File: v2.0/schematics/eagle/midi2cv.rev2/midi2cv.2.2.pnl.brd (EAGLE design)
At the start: 99.4 x 41.9 mm, 22 parts, among them IC1 TL084P, IC2 TL084P, J1 CV3 OUT, J2 CV2 OUT, J3 CV1 OUT, J4 GATE1 OUT, J5 GATE2 OUT, J6 GATE3 OUT, J7 GATE4 OUT, J8 GATE5 OUT

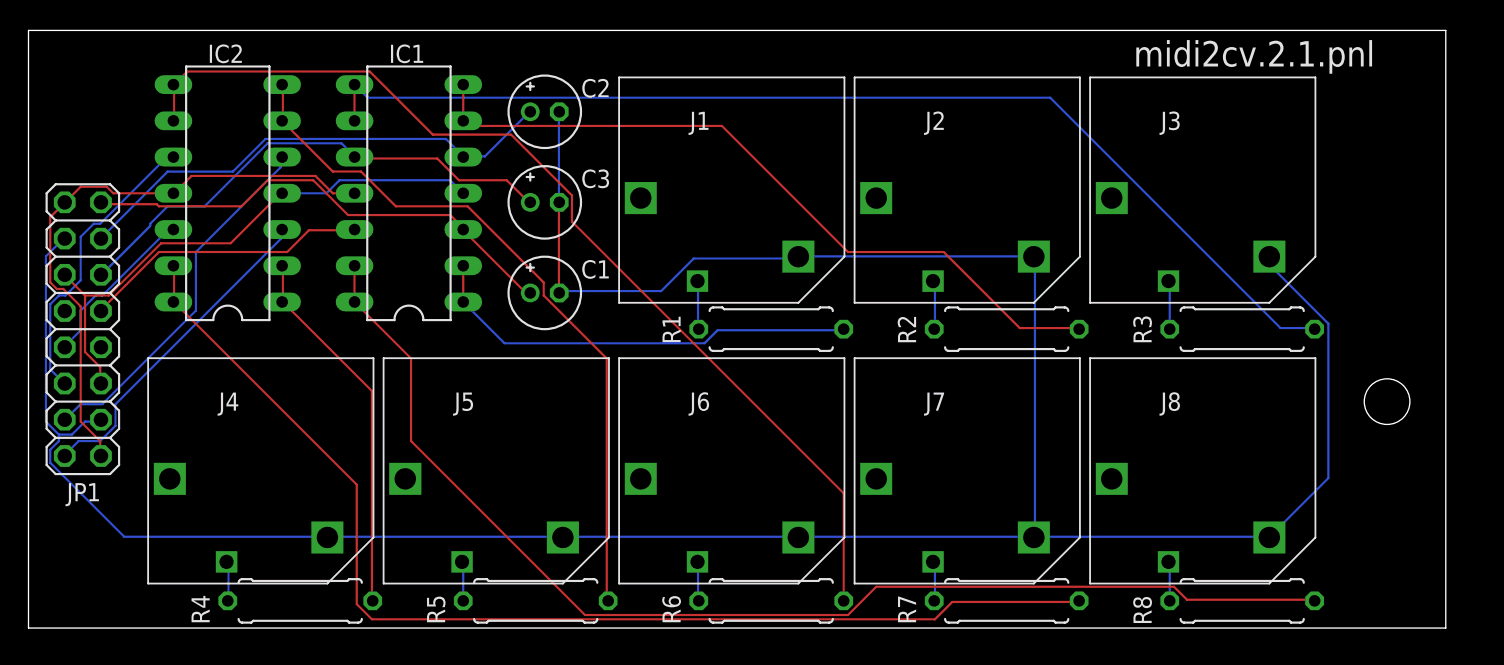
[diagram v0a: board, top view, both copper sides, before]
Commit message: Corrected pin mappings on Jacks Updated midi2cv with new jacks mapping Rerouted main and pnl Increased minimum width in design rules from 6mil to 12mil
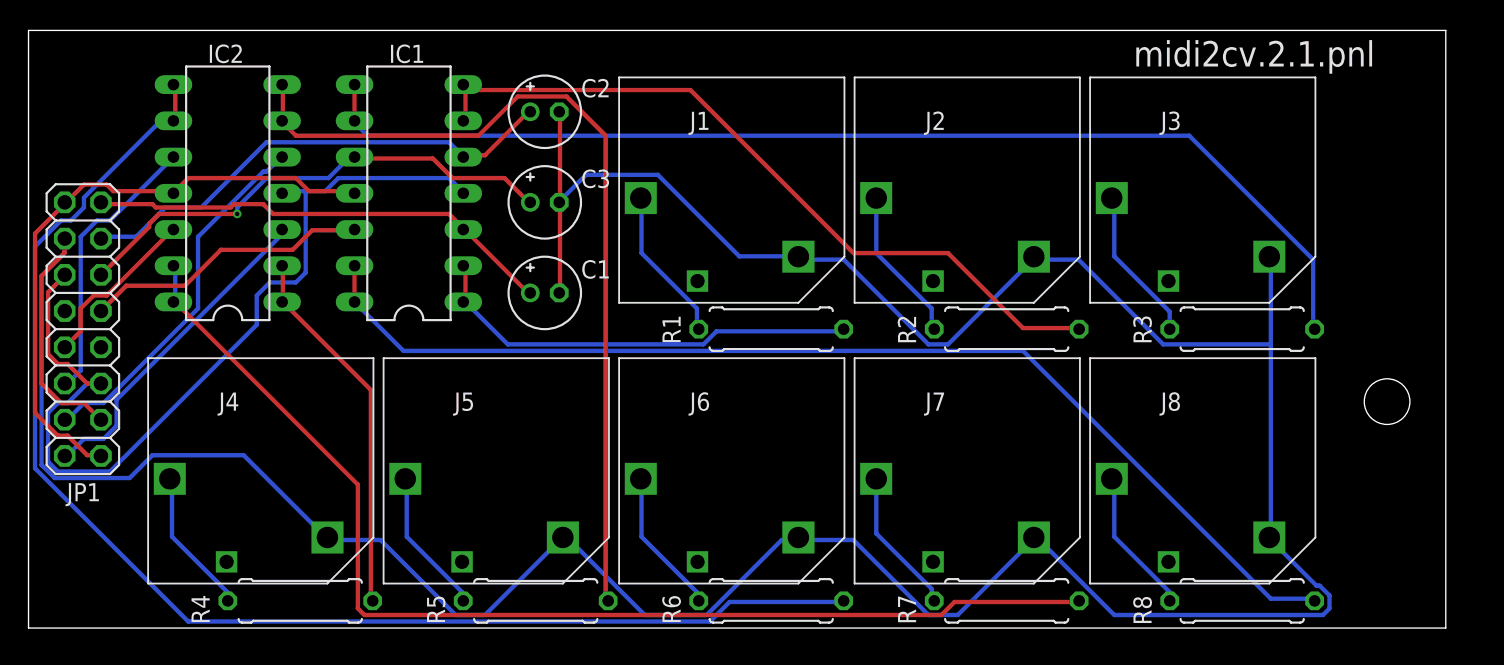
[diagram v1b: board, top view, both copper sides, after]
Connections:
- net N$21: now also J4.P$3; no longer J4.P$2
- net N$22: now also J5.P$3; no longer J5.P$2
- net N$23: now also J6.P$3; no longer J6.P$2
- net N$24: now also J7.P$3; no longer J7.P$2
- net N$25: now also J8.P$3; no longer J8.P$2
- net N$44: now also J1.P$3; no longer J1.P$2
- net N$45: now also J2.P$3; no longer J2.P$2
- net N$46: now also J3.P$3; no longer J3.P$2
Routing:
- net 0V: track 198.0 -> 242.7 mm
- net +12V: track 38.9 -> 63.3 mm
- net N$35: track 70.8 -> 93.7 mm
- net N$36: track 49.8 -> 60.7 mm
- net N$44: track 3.39 -> 10.9 mm
- net N$46: track 3.40 -> 10.9 mm
- net N$25: track 2.78 -> 10.2 mm
- net N$45: track 3.46 -> 10.9 mm
- net N$23: track 2.76 -> 10.2 mm
- net N$22: track 2.78 -> 10.2 mm
- net N$24: track 2.83 -> 10.2 mm
- net N$21: track 2.83 -> 10.2 mm
- net N$7: track 83.6 -> 78.5 mm
- net N$4: track 76.9 -> 78.8 mm
- net -12V: track 41.9 -> 43.6 mm
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
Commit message: Updated version on schem and board to 2.2 Revised labels for GATE1..5 to match board layout and firmare
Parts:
- J4: value GATE1 OUT -> GATE5 OUT
- J5: value GATE2 OUT -> GATE4 OUT
- J7: value GATE4 OUT -> GATE2 OUT
- J8: value GATE5 OUT -> GATE1 OUT
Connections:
- net GATE1: now also IC1.12, JP1.9; no longer IC2.3, JP1.2
- net GATE2: now also IC2.12, JP1.8; no longer IC2.5, JP1.4
- net GATE4: now also IC2.5, JP1.4; no longer IC2.12, JP1.8
- net GATE5: now also IC2.3, JP1.2; no longer IC1.12, JP1.9
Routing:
- net GATE2: track 25.8 -> 11.9 mm
- net GATE4: track 12.0 -> 25.6 mm
- net GATE1: track 23.1 -> 20.1 mm
- net GATE5: track 20.2 -> 22.9 mm
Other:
- board text added: "midi2cv.2.2.pnl"
- board text removed: "midi2cv.2.1.pnl"
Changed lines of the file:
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@@
 <?xml version="1.0" encoding="utf-8"?>
 <!DOCTYPE eagle SYSTEM "eagle.dtd">
-<eagle version="7.5.0">
+<eagle version="7.2.0">
 <drawing>
 <settings>
@@
 <wire x1="99.365" y1="41.9" x2="0" y2="41.9" width="0" layer="20"/>
 <wire x1="0" y1="41.9" x2="0" y2="0" width="0" layer="20"/>
-<text x="77.47" y="39.37" size="1.778" layer="25" font="vector">midi2cv.2.1.pnl</text>
+<text x="77.47" y="39.37" size="1.778" layer="25" font="vector">midi2cv.2.2.pnl</text>
 <hole x="95.25" y="15.875" drill="3.2"/>
 </plain>
@@
 <attribute name="VALUE" x="27.305" y="23.749" size="1.27" layer="27" ratio="10" rot="R90"/>
 </element>
-<element name="J4" library="jacks" package="ACJM-MV35-2S" value="GATE1 OUT" x="20.955" y="6.35" locked="yes"/>
-<element name="J5" library="jacks" package="ACJM-MV35-2S" value="GATE2 OUT" x="37.465" y="6.35" locked="yes"/>
+<element name="J4" library="jacks" package="ACJM-MV35-2S" value="GATE5 OUT" x="20.955" y="6.35" locked="yes"/>
+<element name="J5" library="jacks" package="ACJM-MV35-2S" value="GATE4 OUT" x="37.465" y="6.35" locked="yes"/>
 <element name="J6" library="jacks" package="ACJM-MV35-2S" value="GATE3 OUT" x="53.975" y="6.35" locked="yes"/>
-<element name="J7" library="jacks" package="ACJM-MV35-2S" value="GATE4 OUT" x="70.485" y="6.35" locked="yes"/>
-<element name="J8" library="jacks" package="ACJM-MV35-2S" value="GATE5 OUT" x="86.995" y="6.35" locked="yes"/>
+<element name="J7" library="jacks" package="ACJM-MV35-2S" value="GATE2 OUT" x="70.485" y="6.35" locked="yes"/>
+<element name="J8" library="jacks" package="ACJM-MV35-2S" value="GATE1 OUT" x="86.995" y="6.35" locked="yes"/>
 <element name="J1" library="jacks" package="ACJM-MV35-2S" value="CV3 OUT" x="53.975" y="26.035" locked="yes"/>
 <element name="J2" library="jacks" package="ACJM-MV35-2S" value="CV2 OUT" x="70.485" y="26.035"/>
@@
 <wire x1="76.1238" y1="10.287" x2="75.945" y2="10.46" width="0.3048" layer="16"/>
 </signal>
-<signal name="GATE1">
-<contactref element="JP1" pad="2"/>
-<contactref element="IC2" pad="3"/>
-<wire x1="17.6022" y1="27.432" x2="17.6022" y2="27.8892" width="0.3048" layer="16"/>
-<wire x1="6.1722" y1="16.002" x2="17.6022" y2="27.432" width="0.3048" layer="16"/>
-<wire x1="6.1722" y1="14.1732" x2="6.1722" y2="16.002" width="0.3048" layer="16"/>
-<wire x1="5.2578" y1="13.2588" x2="6.1722" y2="14.1732" width="0.3048" layer="16"/>
-<wire x1="3.8862" y1="13.2588" x2="5.2578" y2="13.2588" width="0.3048" layer="16"/>
-<wire x1="2.7432" y1="12.1158" x2="3.8862" y2="13.2588" width="0.3048" layer="16"/>
-<wire x1="17.6022" y1="27.8892" x2="17.78" y2="27.94" width="0.3048" layer="16"/>
-<wire x1="2.7432" y1="12.1158" x2="2.54" y2="12.065" width="0.3048" layer="16"/>
-</signal>
-<signal name="GATE2">
-<contactref element="JP1" pad="4"/>
-<contactref element="IC2" pad="5"/>
-<wire x1="16.6878" y1="32.004" x2="17.6022" y2="32.9184" width="0.3048" layer="16"/>
-<wire x1="16.4592" y1="32.004" x2="16.6878" y2="32.004" width="0.3048" layer="16"/>
-<wire x1="11.8872" y1="27.432" x2="16.4592" y2="32.004" width="0.3048" layer="16"/>
-<wire x1="11.8872" y1="22.4028" x2="11.8872" y2="27.432" width="0.3048" layer="16"/>
-<wire x1="5.2578" y1="15.7734" x2="11.8872" y2="22.4028" width="0.3048" layer="16"/>
-<wire x1="3.8862" y1="15.7734" x2="5.2578" y2="15.7734" width="0.3048" layer="16"/>
-<wire x1="2.7432" y1="14.6304" x2="3.8862" y2="15.7734" width="0.3048" layer="16"/>
-<wire x1="17.6022" y1="32.9184" x2="17.78" y2="33.02" width="0.3048" layer="16"/>
-<wire x1="2.7432" y1="14.6304" x2="2.54" y2="14.605" width="0.3048" layer="16"/>
-</signal>
 <signal name="GATE3">
 <contactref element="JP1" pad="6"/>
@@
 <wire x1="2.7432" y1="17.145" x2="3.6576" y2="18.0594" width="0.3048" layer="16"/>
 <wire x1="2.7432" y1="17.145" x2="2.54" y2="17.145" width="0.3048" layer="16"/>
-</signal>
-<signal name="GATE4">
-<contactref element="JP1" pad="8"/>
-<contactref element="IC2" pad="12"/>
-<wire x1="5.4864" y1="23.3172" x2="10.0584" y2="27.8892" width="0.3048" layer="1"/>
-<wire x1="4.572" y1="23.3172" x2="5.4864" y2="23.3172" width="0.3048" layer="1"/>
-<wire x1="3.6576" y1="22.4028" x2="4.572" y2="23.3172" width="0.3048" layer="1"/>
-<wire x1="3.6576" y1="20.8026" x2="3.6576" y2="22.4028" width="0.3048" layer="1"/>
-<wire x1="2.54" y1="19.685" x2="3.6576" y2="20.8026" width="0.3048" layer="1"/>
-<wire x1="10.0584" y1="27.8892" x2="10.16" y2="27.94" width="0.3048" layer="1"/>
-</signal>
-<signal name="GATE5">
-<contactref element="JP1" pad="9"/>
-<contactref element="IC1" pad="12"/>
-<wire x1="19.8882" y1="27.8892" x2="22.86" y2="27.8892" width="0.3048" layer="1"/>
-<wire x1="18.5166" y1="26.5176" x2="19.8882" y2="27.8892" width="0.3048" layer="1"/>
-<wire x1="13.4874" y1="26.5176" x2="18.5166" y2="26.5176" width="0.3048" layer="1"/>
-<wire x1="10.9728" y1="24.003" x2="13.4874" y2="26.5176" width="0.3048" layer="1"/>
-<wire x1="6.858" y1="24.003" x2="10.9728" y2="24.003" width="0.3048" layer="1"/>
-<wire x1="5.08" y1="22.225" x2="6.858" y2="24.003" width="0.3048" layer="1"/>
-<wire x1="22.86" y1="27.8892" x2="22.86" y2="27.94" width="0.3048" layer="1"/>
 </signal>
 <signal name="CV2">
@@
 <via x="14.6304" y="29.0322" extent="1-16" drill="0.3048"/>
 </signal>
+<signal name="GATE5">
+<contactref element="IC2" pad="3"/>
+<contactref element="JP1" pad="2"/>
+<wire x1="17.6022" y1="27.432" x2="17.6022" y2="27.8892" width="0.3048" layer="16"/>
+<wire x1="6.1722" y1="16.002" x2="17.6022" y2="27.432" width="0.3048" layer="16"/>
+<wire x1="6.1722" y1="14.1732" x2="6.1722" y2="16.002" width="0.3048" layer="16"/>
+<wire x1="5.2578" y1="13.2588" x2="6.1722" y2="14.1732" width="0.3048" layer="16"/>
+<wire x1="3.8862" y1="13.2588" x2="5.2578" y2="13.2588" width="0.3048" layer="16"/>
+<wire x1="2.7432" y1="12.1158" x2="3.8862" y2="13.2588" width="0.3048" layer="16"/>
+<wire x1="2.7432" y1="12.1158" x2="2.54" y2="12.065" width="0.3048" layer="16"/>
+<wire x1="17.6022" y1="27.8892" x2="17.78" y2="27.94" width="0" layer="19" extent="16-16"/>
+</signal>
+<signal name="GATE4">
+<contactref element="IC2" pad="5"/>
+<contactref element="JP1" pad="4"/>
+<wire x1="16.6878" y1="32.004" x2="17.6022" y2="32.9184" width="0.3048" layer="16"/>
+<wire x1="16.4592" y1="32.004" x2="16.6878" y2="32.004" width="0.3048" layer="16"/>
+<wire x1="11.8872" y1="27.432" x2="16.4592" y2="32.004" width="0.3048" layer="16"/>
+<wire x1="11.8872" y1="22.4028" x2="11.8872" y2="27.432" width="0.3048" layer="16"/>
+<wire x1="5.2578" y1="15.7734" x2="11.8872" y2="22.4028" width="0.3048" layer="16"/>
+<wire x1="3.8862" y1="15.7734" x2="5.2578" y2="15.7734" width="0.3048" layer="16"/>
+<wire x1="2.7432" y1="14.6304" x2="3.8862" y2="15.7734" width="0.3048" layer="16"/>
+<wire x1="2.7432" y1="14.6304" x2="2.54" y2="14.605" width="0.3048" layer="16"/>
+<wire x1="17.6022" y1="32.9184" x2="17.78" y2="33.02" width="0" layer="19" extent="16-16"/>
+</signal>
+<signal name="GATE2">
+<contactref element="IC2" pad="12"/>
+<contactref element="JP1" pad="8"/>
+<wire x1="5.4864" y1="23.3172" x2="10.0584" y2="27.8892" width="0.3048" layer="1"/>
+<wire x1="4.572" y1="23.3172" x2="5.4864" y2="23.3172" width="0.3048" layer="1"/>
+<wire x1="3.6576" y1="22.4028" x2="4.572" y2="23.3172" width="0.3048" layer="1"/>
+<wire x1="3.6576" y1="20.8026" x2="3.6576" y2="22.4028" width="0.3048" layer="1"/>
+<wire x1="2.54" y1="19.685" x2="3.6576" y2="20.8026" width="0.3048" layer="1"/>
+<wire x1="10.0584" y1="27.8892" x2="10.16" y2="27.94" width="0" layer="19" extent="1-1"/>
+</signal>
+<signal name="GATE1">
+<contactref element="IC1" pad="12"/>
+<contactref element="JP1" pad="9"/>
+<wire x1="19.8882" y1="27.8892" x2="22.86" y2="27.8892" width="0.3048" layer="1"/>
+<wire x1="18.5166" y1="26.5176" x2="19.8882" y2="27.8892" width="0.3048" layer="1"/>
+<wire x1="13.4874" y1="26.5176" x2="18.5166" y2="26.5176" width="0.3048" layer="1"/>
+<wire x1="10.9728" y1="24.003" x2="13.4874" y2="26.5176" width="0.3048" layer="1"/>
+<wire x1="6.858" y1="24.003" x2="10.9728" y2="24.003" width="0.3048" layer="1"/>
+<wire x1="5.08" y1="22.225" x2="6.858" y2="24.003" width="0.3048" layer="1"/>
+<wire x1="22.86" y1="27.8892" x2="22.86" y2="27.94" width="0" layer="19" extent="1-1"/>
+</signal>
 </signals>
